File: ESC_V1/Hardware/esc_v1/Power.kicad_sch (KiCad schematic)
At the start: 22 parts, among them U1 AZ1117CH-5.0TRG1, U2 AZ1117CH-3.3TRG1, U3 TPS5450DDAR

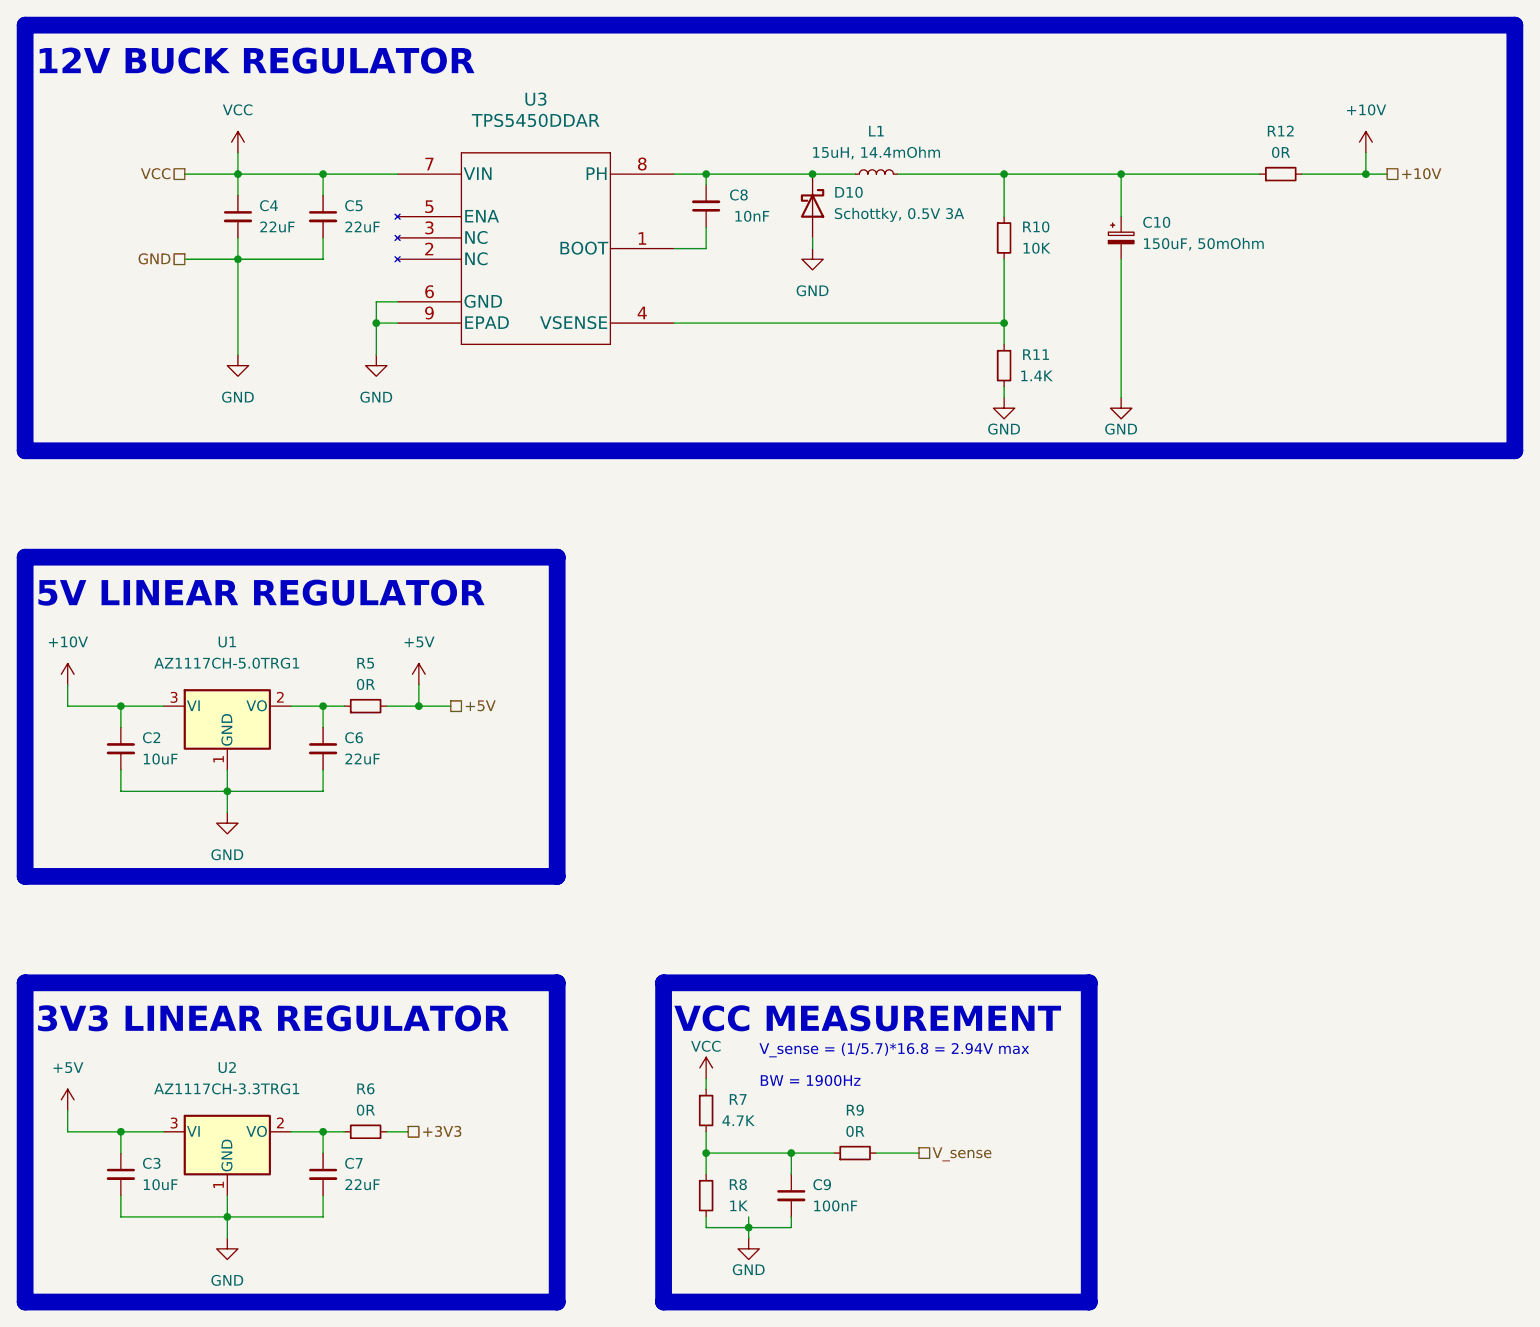
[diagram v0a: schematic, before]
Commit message: Components roughly placed in layout
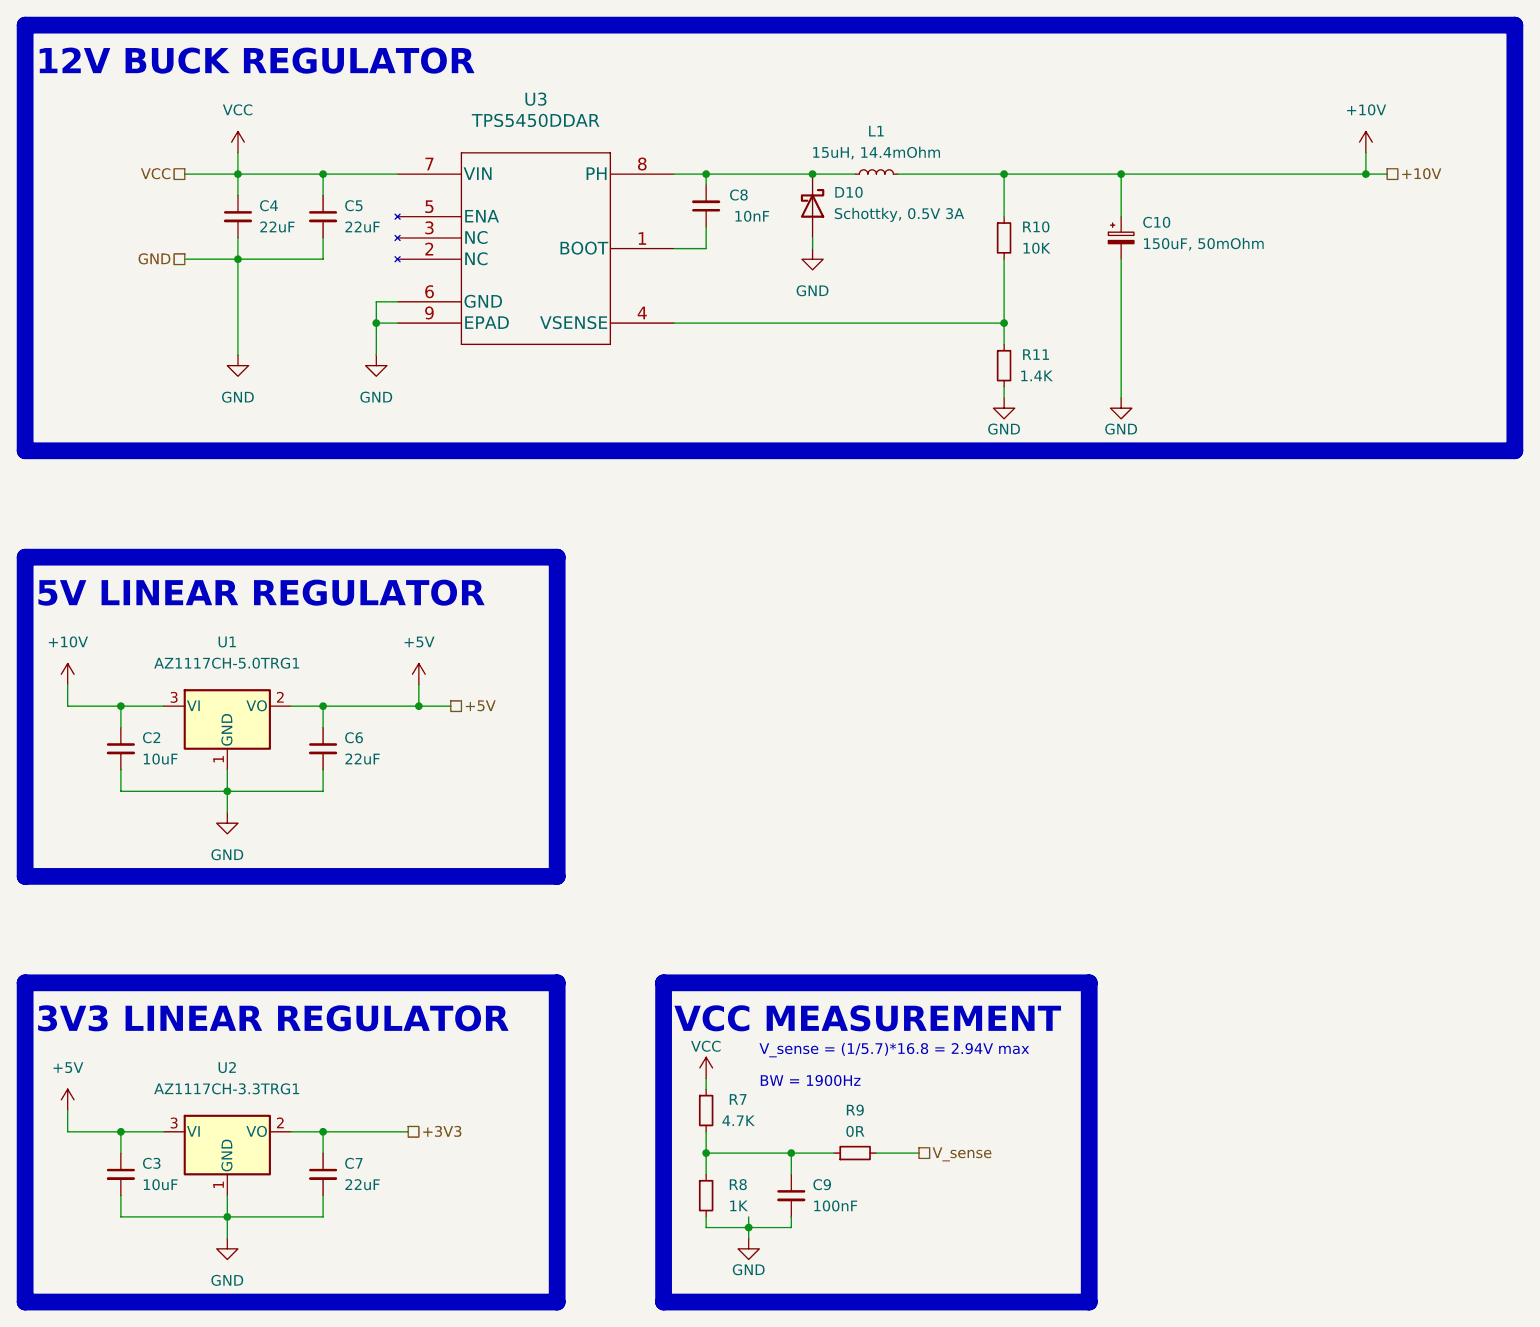
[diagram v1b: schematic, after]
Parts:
- removed R12, R5, R6: 0R, Resistor_SMD:R_0603_1608Metric, symbol Device:R_Small
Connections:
- net +10V: now also C10.1, L1.2, R10.1
- net +3V3: now also C7.1, U2.2 (VO)
- net +5V: now also C6.1, U1.2 (VO)
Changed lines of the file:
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@@
-    (stroke (width 0) (type default) (color 0 0 0 0))
-  )
-  (wire (pts (xy 60.96 157.48) (xy 63.5 157.48))
     (stroke (width 0) (type default) (color 0 0 0 0))
   )
@@
     (stroke (width 0) (type default) (color 0 0 0 0))
   )
-  (wire (pts (xy 156.21 43.18) (xy 172.72 43.18))
-    (stroke (width 0) (type default) (color 0 0 0 0))
-  )
   (wire (pts (xy 142.24 60.96) (xy 142.24 63.5))
     (stroke (width 0) (type default) (color 0 0 0 0))
@@
     (stroke (width 0) (type default) (color 0 0 0 0))
   )
-  (wire (pts (xy 60.96 106.68) (xy 63.5 106.68))
-    (stroke (width 0) (type default) (color 0 0 0 0))
-  )
   (wire (pts (xy 106.68 52.07) (xy 102.87 52.07))
     (stroke (width 0) (type default) (color 0 0 0 0))
@@
     (stroke (width 0) (type default) (color 0 0 0 0))
   )
-  (wire (pts (xy 68.58 106.68) (xy 72.39 106.68))
+  (wire (pts (xy 60.96 106.68) (xy 72.39 106.68))
     (stroke (width 0) (type default) (color 0 0 0 0))
   )
@@
     (stroke (width 0) (type default) (color 0 0 0 0))
   )
-  (wire (pts (xy 177.8 43.18) (xy 185.42 43.18))
+  (wire (pts (xy 156.21 43.18) (xy 185.42 43.18))
     (stroke (width 0) (type default) (color 0 0 0 0))
   )
@@
     (stroke (width 0) (type default) (color 0 0 0 0))
   )
-  (wire (pts (xy 68.58 157.48) (xy 71.12 157.48))
+  (wire (pts (xy 60.96 157.48) (xy 71.12 157.48))
     (stroke (width 0) (type default) (color 0 0 0 0))
   )
@@
     )
     (pin "1")
-  )
-  (symbol (lib_id "Device:R_Small") (at 66.04 157.48 90) (unit 1)
-    (in_bom yes) (on_board yes)
-    (property "Reference" "R6" (id 0) (at 66.04 152.4 90))
-    (property "Value" "0R" (id 1) (at 66.04 154.94 90))
-    (property "Footprint" "Resistor_SMD:R_0603_1608Metric" (id 2) (at 66.04 157.48 0)
-      (effects (font (size 1.27 1.27)) hide)
-    )
-    (property "Datasheet" "~" (id 3) (at 66.04 157.48 0)
-      (effects (font (size 1.27 1.27)) hide)
-    )
-    (pin "1")
-    (pin "2")
   )
   (symbol (lib_id "power:VCC") (at 50.8 40.64 0) (unit 1)
@@
     (pin "2")
   )
-  (symbol (lib_id "Device:R_Small") (at 175.26 43.18 90) (unit 1)
-    (in_bom yes) (on_board yes)
-    (property "Reference" "R12" (id 0) (at 175.26 38.1 90))
-    (property "Value" "0R" (id 1) (at 175.26 40.64 90))
-    (property "Footprint" "Resistor_SMD:R_0603_1608Metric" (id 2) (at 175.26 43.18 0)
-      (effects (font (size 1.27 1.27)) hide)
-    )
-    (property "Datasheet" "~" (id 3) (at 175.26 43.18 0)
-      (effects (font (size 1.27 1.27)) hide)
-    )
-    (pin "1")
-    (pin "2")
-  )
   (symbol (lib_id "power:GND") (at 67.31 64.77 0) (unit 1)
     (in_bom yes) (on_board yes) (fields_autoplaced)
@@
     (pin "1")
   )
-  (symbol (lib_id "Device:R_Small") (at 66.04 106.68 90) (unit 1)
-    (in_bom yes) (on_board yes)
-    (property "Reference" "R5" (id 0) (at 66.04 101.6 90))
-    (property "Value" "0R" (id 1) (at 66.04 104.14 90))
-    (property "Footprint" "Resistor_SMD:R_0603_1608Metric" (id 2) (at 66.04 106.68 0)
-      (effects (font (size 1.27 1.27)) hide)
-    )
-    (property "Datasheet" "~" (id 3) (at 66.04 106.68 0)
-      (effects (font (size 1.27 1.27)) hide)
-    )
-    (pin "1")
-    (pin "2")
-  )
   (symbol (lib_id "power:GND") (at 49.53 170.18 0) (unit 1)
